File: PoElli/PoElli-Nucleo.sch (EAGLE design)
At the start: 116 parts, among them J3 M022.54MM, J4 M022.54MM, Q3 FDMC2674HANDSOLDERING, Q4 FDMC2674HANDSOLDERING, T1 Coilcraft 230NL, U4 LT3748, U5 TPS2378, U6 ENC424J600, X1 POE-TP-SHIELDED-LEDSTE1888250, Y1 25 MHz

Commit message: tentative layout
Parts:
- removed D10, D14, D15, D16, D17, D7, D8, D9: B2100, ELL-i-DIscreteSemi:DIODE-SCHOTTKYB2100
- added C10: 1nF 2kV, ELL-i-Passives:C1206-A
- added C3: 100nF, ELL-i-Passives:C0805-A
- added U$3, U$4: BRIDGE-RECTIFIER, ELL-i-DIscreteSemi:BRIDGE-RECTIFIER
- C11, C15: device ELL-i-Passives:C0402 -> ELL-i-Passives:C0402-B
- C34: device ELL-i-Passives:C0402-B -> ELL-i-Passives:C0805-A
- R23, R5: device ELL-i-Passives:R0603 -> ELL-i-Passives:R0805-A
- R29: device ELL-i-Passives:R0805 -> ELL-i-Passives:R0805-A
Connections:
- new net N$9: C10.1, R20.1, R21.1
- net ENC-3V3: now also C3.2
- net GNDA: now also C3.1
- net N$5: no longer R20.1, R21.1
- net N$6: now also U$3.+, U$4.+; no longer D10.C, D7.C, D8.C, D9.C
- net N$8: now also U$3.-, U$4.-; no longer D14.A, D15.A, D16.A, D17.A
- net POE_A+: now also U$3.AC1; no longer D14.C, D7.A
- net POE_A-: now also U$3.AC2; no longer D15.C, D8.A
- net POE_B+: now also U$4.AC1; no longer D10.A, D17.C
- net POE_B-: now also U$4.AC2; no longer D16.C, D9.A
- net SGND: now also C10.2
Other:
- note added: "Separate ESD protection for easier layout"

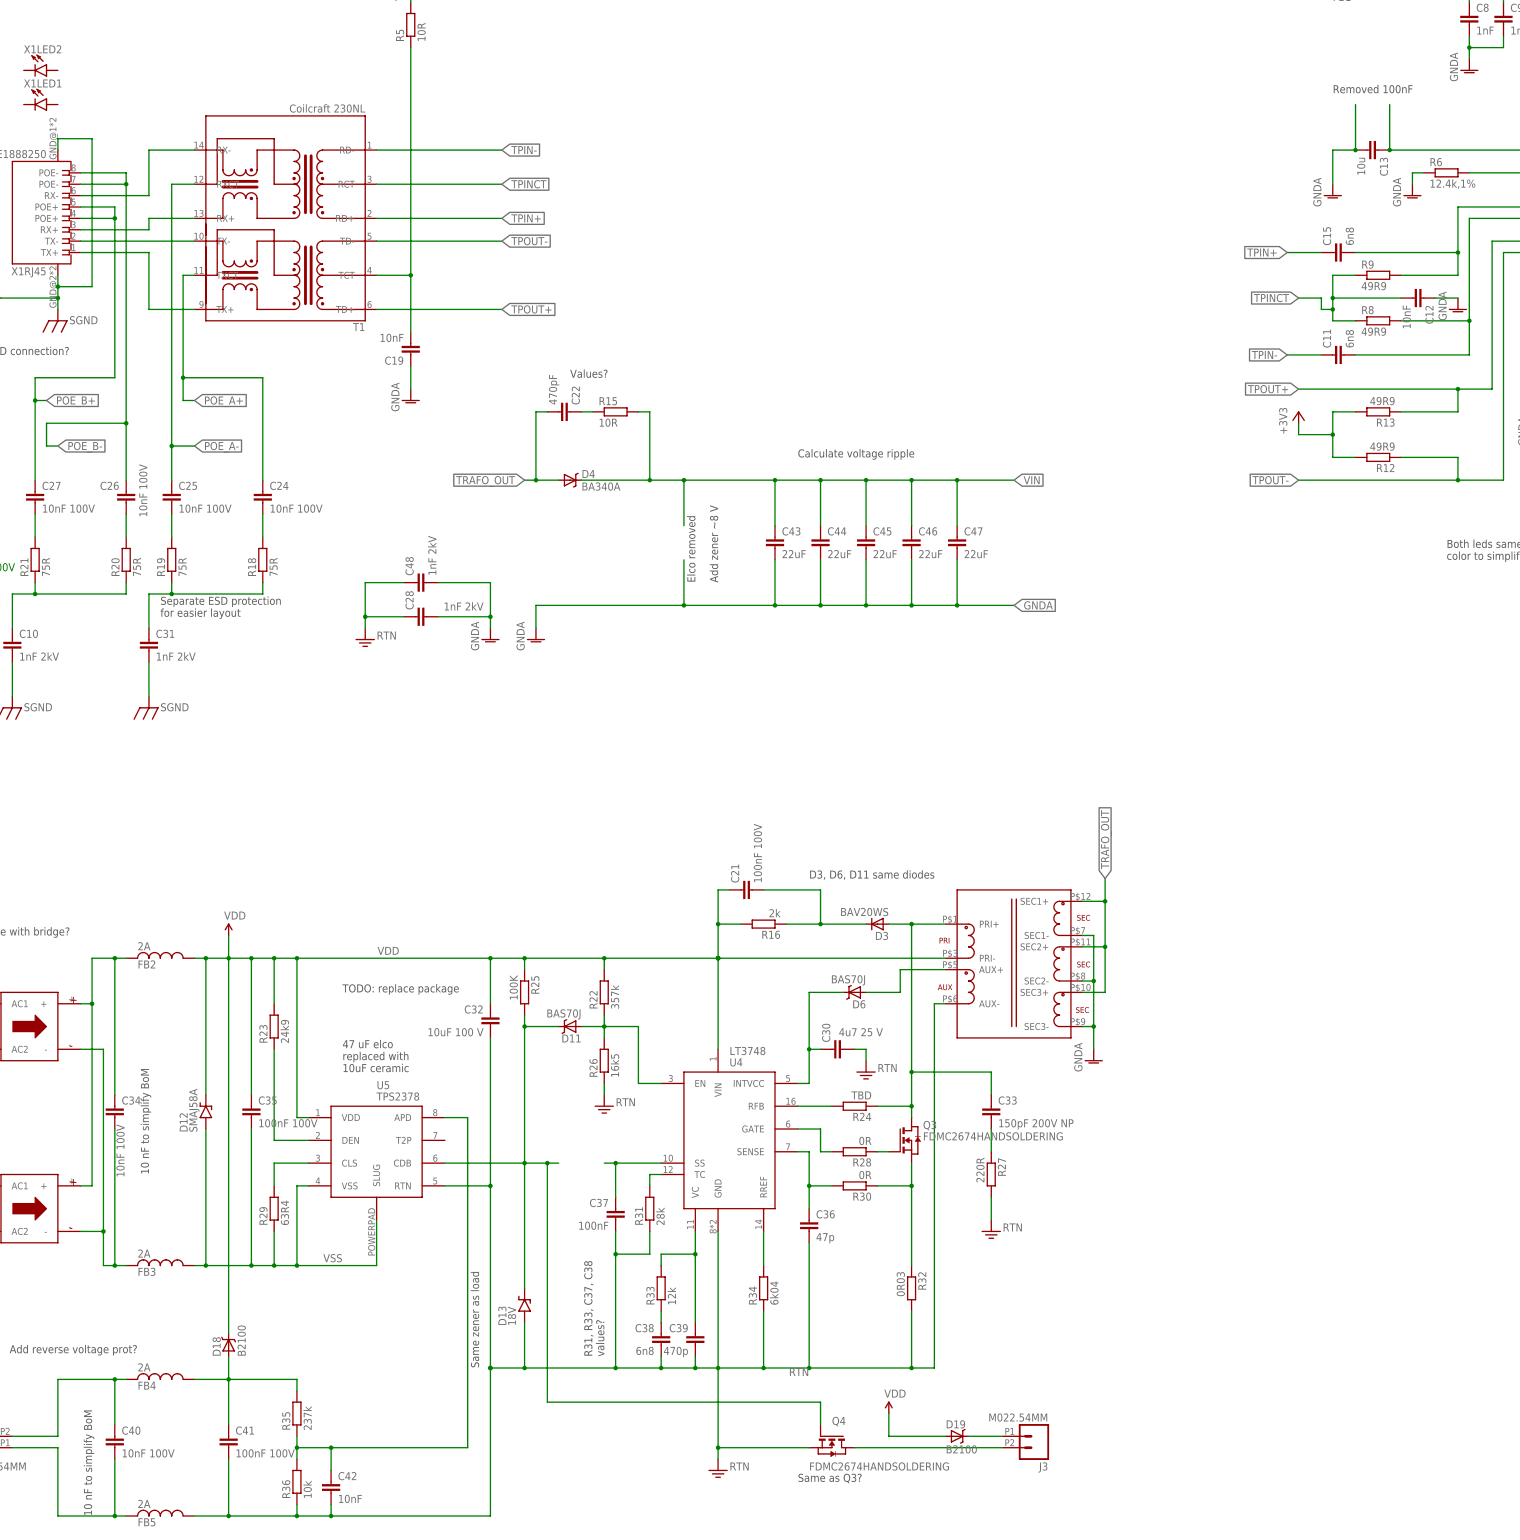
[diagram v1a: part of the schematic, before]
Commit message: Layout, functional blocks placed down
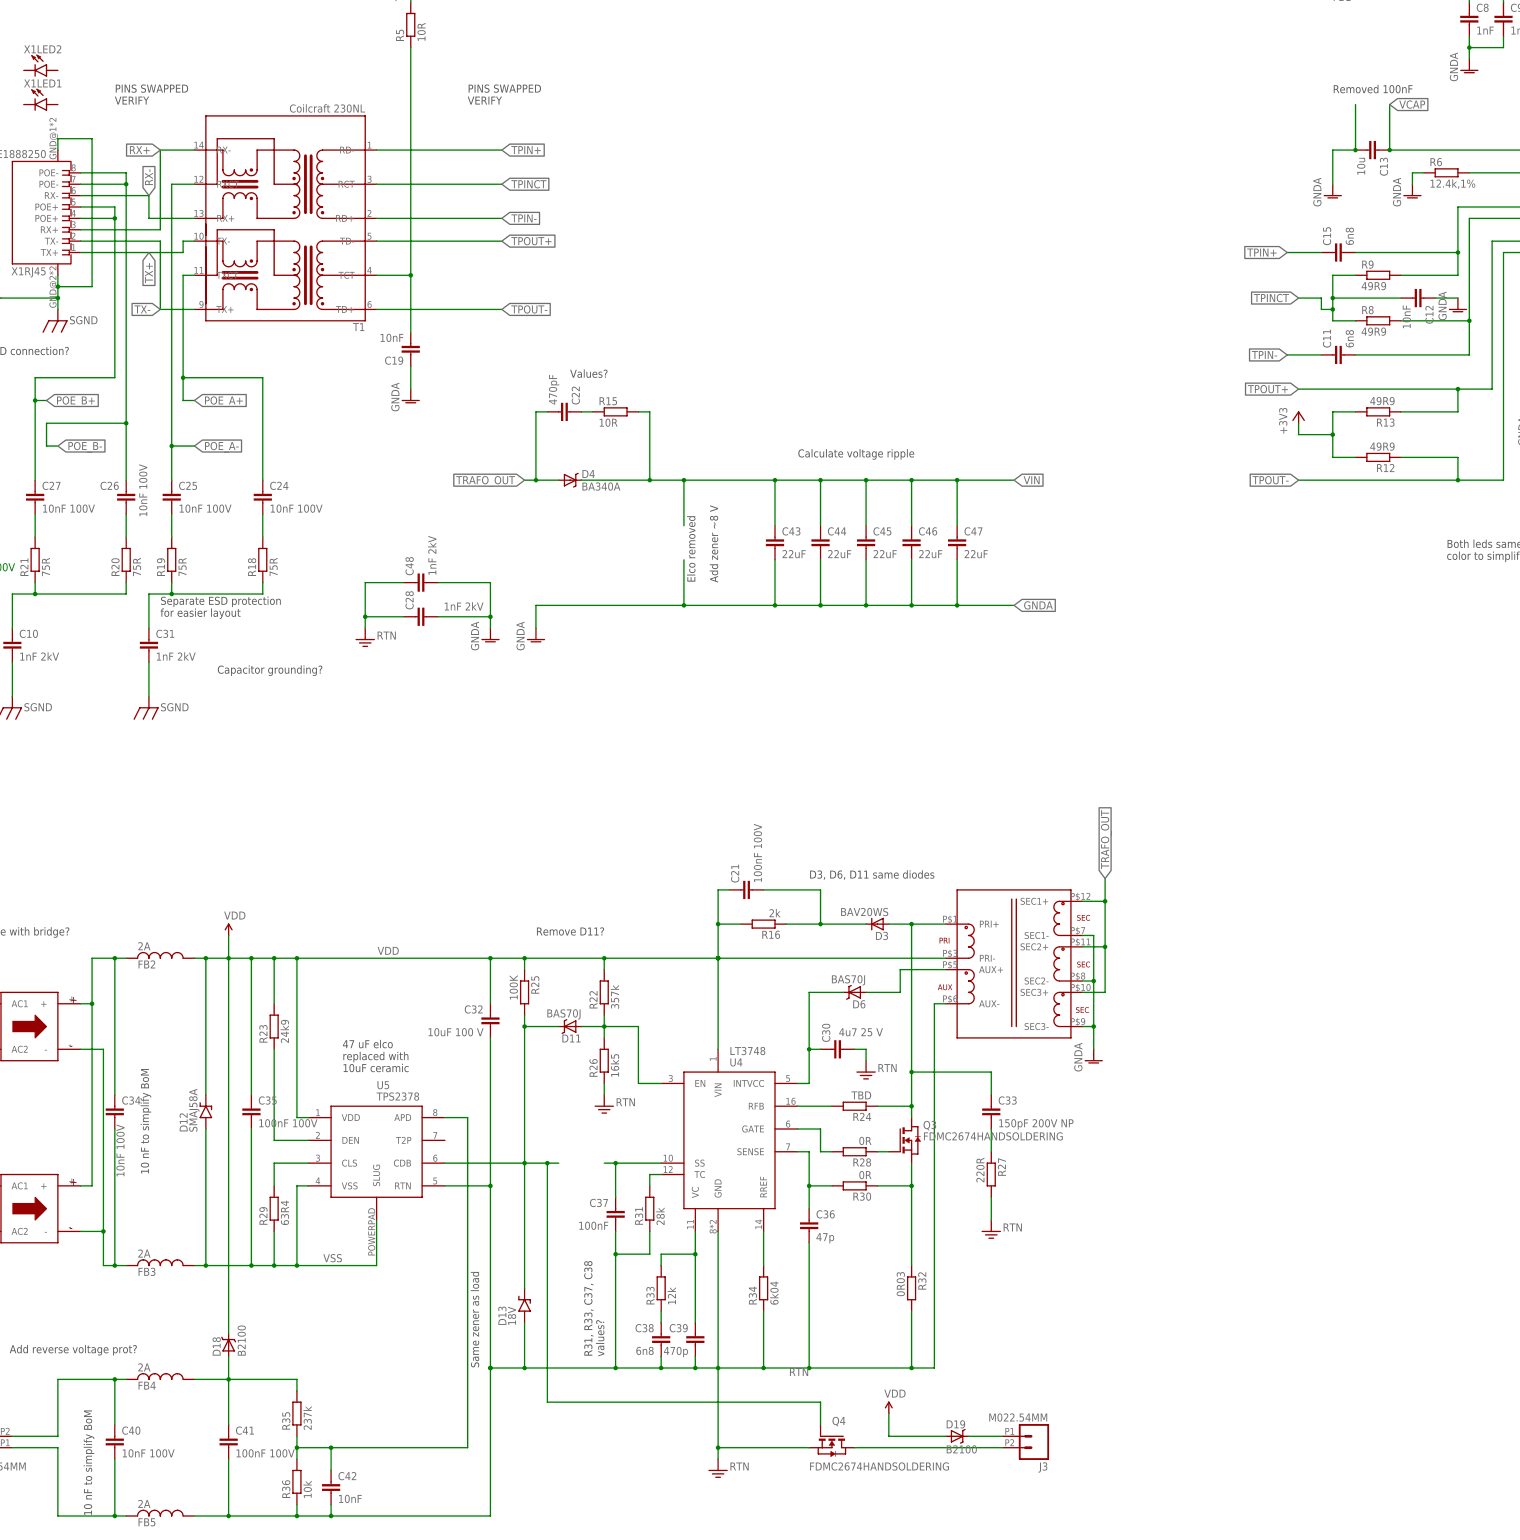
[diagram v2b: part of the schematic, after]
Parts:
- C11, C15: device ELL-i-Passives:C0402-B -> ELL-i-Passives:C0805-A
- C21: device ELL-i-Passives:C0805 -> ELL-i-Passives:C0805-A
- C28, C48: device ELL-i-Passives:CC1206 -> ELL-i-Passives:C1206-A
- C32: device ELL-i-Passives:C1206-A -> ELL-i-Passives:C2220-REFLOW
- FB1: device ELL-i-Passives:FB0402 -> ELL-i-Passives:FB-0805-A
- FB2, FB3, FB5: device ELL-i-Passives:FB1206 -> ELL-i-Passives:FB-0805-A
- FB4: device ELL-i-Passives:FB1206 -> ELL-i-Passives:FB-0603-A
- R16: device ELL-i-Passives:R1206 -> ELL-i-Passives:R1206-A
- R22, R25, R26: device ELL-i-Passives:R0603 -> ELL-i-Passives:R0805-A
- R32: device ELL-i-Passives:R0805 -> ELL-i-Passives:R0805-A
- renumbered U$1 to T2, U$3 to B1, U$4 to B2
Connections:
- removed net N$1: T1.TX-, X1RJ45.TX-@2
- removed net N$2: T1.TX+, X1RJ45.TX+@1
- removed net N$3: T1.RX+, X1RJ45.RX+@3
- removed net N$4: T1.RX-, X1RJ45.RX-@6
- new net RX+: T1.RX-, X1RJ45.RX+@3
- new net RX-: T1.RX+, X1RJ45.RX-@6
- new net TX+: T1.TX-, X1RJ45.TX+@1
- new net TX-: T1.TX+, X1RJ45.TX-@2
- net TPIN+: now also T1.RD-; no longer T1.RD+
- net TPIN-: now also T1.RD+; no longer T1.RD-
- net TPOUT+: now also T1.TD-; no longer T1.TD+
- net TPOUT-: now also T1.TD+; no longer T1.TD-
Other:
- note added: "Capacitor grounding?"
- note added: "PINS SWAPPED VERIFY"
- note added: "Remove D11?"
- note removed: "Same as Q3?"
- note removed: "TODO: replace package"

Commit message: Component placement almost ready
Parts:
- removed C31: 1nF 2kV, ELL-i-Passives:C1206-A
- removed C36: 47p, ELL-i-Passives:C0805-A
- removed D11: BAS70J, ELL-i-DIscreteSemi:BAS70J
- removed R25: 100K, ELL-i-Passives:R0805-A
- removed R30: 0R, ELL-i-Passives:R0805-A
- C1, C11, C12, C13, C15, C2, C21, C22, C24, C25, C26, C27, C3, C30, C33, C34, C35, C37, C38, C39, C4, C41, C42, C5, C6, C7: device ELL-i-Passives:C0805-A -> ELL-i-Passives:C0603-B
- FB2, FB3, FB5: device ELL-i-Passives:FB-0805-A -> ELL-i-Passives:FB-0603-A
- R12, R13, R15, R18, R19, R20, R21, R22, R23, R24, R26, R27, R28, R29, R33, R35, R36, R6, R8, R9: device ELL-i-Passives:R0805-A -> ELL-i-Passives:R0603-B
- R32: value 0R03 -> 0R10; device ELL-i-Passives:R0805-A -> ELL-i-Passives:R0603-B
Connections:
- removed net N$27: Q3.S, R30.1, R32.1
- removed net N$9: C10.1, R20.1, R21.1
- removed net U5_CDB: D11.C, D13.C, Q4.G, R25.2, U5.CDB
- net GNDA: now also C10.2
- net N$26: now also Q3.S, R32.1; no longer C36.1, R30.2
- net N$5: now also C10.1, R20.1, R21.1; no longer C31.1
- net RTN: no longer C36.2
- net SGND: no longer C10.2, C31.2
- net U4_EN: now also D13.C, Q4.G, U5.CDB; no longer D11.A
- net VDD: no longer R25.1
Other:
- note added: "Ilim = 1A"
- note added: "Recalculate R22"
- note added: "Removed R25, D11"
- note added: "Removed RC"
- note added: "SGND left floating"
- note removed: "Remove D11?"
- note removed: "SGND connection?"
- note removed: "Separate ESD protection for easier layout"

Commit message: DC/DC layout except planes
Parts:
- C19: device ELL-i-Passives:C0805-A -> ELL-i-Passives:C0603-B
- R3, R4: device ELL-i-Passives:R0805-A -> ELL-i-Passives:R0603-A
- R31, R34, R5: device ELL-i-Passives:R0805-A -> ELL-i-Passives:R0603-B
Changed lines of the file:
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@@
 <grid distance="0.1" unitdist="inch" unit="inch" style="lines" multiple="1" display="no" altdistance="0.01" altunitdist="inch" altunit="inch"/>
 <layers>
-<layer number="1" name="Top" color="4" fill="1" visible="yes" active="no"/>
-<layer number="2" name="Route2" color="4" fill="15" visible="yes" active="no"/>
-<layer number="3" name="Route3" color="4" fill="3" visible="yes" active="no"/>
-<layer number="14" name="Route14" color="1" fill="6" visible="yes" active="no"/>
-<layer number="15" name="Route15" color="1" fill="15" visible="yes" active="no"/>
-<layer number="16" name="Bottom" color="1" fill="1" visible="yes" active="no"/>
-<layer number="17" name="Pads" color="2" fill="1" visible="yes" active="no"/>
-<layer number="18" name="Vias" color="2" fill="1" visible="yes" active="no"/>
-<layer number="19" name="Unrouted" color="6" fill="1" visible="yes" active="no"/>
-<layer number="20" name="Dimension" color="15" fill="1" visible="yes" active="no"/>
-<layer number="21" name="tPlace" color="11" fill="1" visible="yes" active="no"/>
-<layer number="22" name="bPlace" color="7" fill="1" visible="yes" active="no"/>
-<layer number="23" name="tOrigins" color="15" fill="1" visible="yes" active="no"/>
-<layer number="24" name="bOrigins" color="15" fill="1" visible="yes" active="no"/>
-<layer number="25" name="tNames" color="11" fill="1" visible="yes" active="no"/>
-<layer number="26" name="bNames" color="7" fill="1" visible="yes" active="no"/>
-<layer number="27" name="tValues" color="7" fill="1" visible="yes" active="no"/>
-<layer number="28" name="bValues" color="7" fill="1" visible="yes" active="no"/>
+<layer number="1" name="Top" color="4" fill="1" visible="no" active="no"/>
+<layer number="2" name="Route2" color="4" fill="15" visible="no" active="no"/>
+<layer number="3" name="Route3" color="4" fill="3" visible="no" active="no"/>
+<layer number="14" name="Route14" color="1" fill="6" visible="no" active="no"/>
+<layer number="15" name="Route15" color="1" fill="15" visible="no" active="no"/>
+<layer number="16" name="Bottom" color="1" fill="1" visible="no" active="no"/>
+<layer number="17" name="Pads" color="2" fill="1" visible="no" active="no"/>
+<layer number="18" name="Vias" color="2" fill="1" visible="no" active="no"/>
+<layer number="19" name="Unrouted" color="6" fill="1" visible="no" active="no"/>
+<layer number="20" name="Dimension" color="15" fill="1" visible="no" active="no"/>
+<layer number="21" name="tPlace" color="11" fill="1" visible="no" active="no"/>
+<layer number="22" name="bPlace" color="7" fill="1" visible="no" active="no"/>
+<layer number="23" name="tOrigins" color="15" fill="1" visible="no" active="no"/>
+<layer number="24" name="bOrigins" color="15" fill="1" visible="no" active="no"/>
+<layer number="25" name="tNames" color="11" fill="1" visible="no" active="no"/>
+<layer number="26" name="bNames" color="7" fill="1" visible="no" active="no"/>
+<layer number="27" name="tValues" color="7" fill="1" visible="no" active="no"/>
+<layer number="28" name="bValues" color="7" fill="1" visible="no" active="no"/>
 <layer number="29" name="tStop" color="7" fill="3" visible="no" active="no"/>
 <layer number="30" name="bStop" color="7" fill="6" visible="no" active="no"/>
@@
 <layer number="35" name="tGlue" color="7" fill="4" visible="no" active="no"/>
 <layer number="36" name="bGlue" color="7" fill="5" visible="no" active="no"/>
-<layer number="37" name="tTest" color="7" fill="1" visible="yes" active="no"/>
-<layer number="38" name="bTest" color="7" fill="1" visible="yes" active="no"/>
+<layer number="37" name="tTest" color="7" fill="1" visible="no" active="no"/>
+<layer number="38" name="bTest" color="7" fill="1" visible="no" active="no"/>
 <layer number="39" name="tKeepout" color="4" fill="11" visible="no" active="no"/>
 <layer number="40" name="bKeepout" color="1" fill="11" visible="no" active="no"/>
@@
 <layer number="44" name="Drills" color="7" fill="1" visible="no" active="no"/>
 <layer number="45" name="Holes" color="7" fill="1" visible="no" active="no"/>
-<layer number="46" name="Milling" color="3" fill="1" visible="yes" active="no"/>
-<layer number="47" name="Measures" color="8" fill="1" visible="yes" active="no"/>
-<layer number="48" name="Document" color="7" fill="1" visible="yes" active="no"/>
-<layer number="49" name="Reference" color="7" fill="1" visible="yes" active="no"/>
-<layer number="50" name="dxf" color="7" fill="1" visible="yes" active="no"/>
-<layer number="51" name="tDocu" color="1" fill="1" visible="yes" active="no"/>
-<layer number="52" name="bDocu" color="7" fill="1" visible="yes" active="no"/>
-<layer number="53" name="tGND_GNDA" color="7" fill="9" visible="yes" active="no"/>
-<layer number="54" name="bGND_GNDA" color="1" fill="9" visible="yes" active="no"/>
-<layer number="56" name="wert" color="7" fill="1" visible="yes" active="no"/>
-<layer number="57" name="tCopper" color="7" fill="1" visible="yes" active="no"/>
-<layer number="58" name="bCopper" color="7" fill="1" visible="yes" active="no"/>
+<layer number="46" name="Milling" color="3" fill="1" visible="no" active="no"/>
+<layer number="47" name="Measures" color="8" fill="1" visible="no" active="no"/>
+<layer number="48" name="Document" color="7" fill="1" visible="no" active="no"/>
+<layer number="49" name="Reference" color="7" fill="1" visible="no" active="no"/>
+<layer number="50" name="dxf" color="7" fill="1" visible="no" active="no"/>
+<layer number="51" name="tDocu" color="1" fill="1" visible="no" active="no"/>
+<layer number="52" name="bDocu" color="7" fill="1" visible="no" active="no"/>
+<layer number="53" name="tGND_GNDA" color="7" fill="9" visible="no" active="no"/>
+<layer number="54" name="bGND_GNDA" color="1" fill="9" visible="no" active="no"/>
+<layer number="56" name="wert" color="7" fill="1" visible="no" active="no"/>
+<layer number="57" name="tCopper" color="7" fill="1" visible="no" active="no"/>
+<layer number="58" name="bCopper" color="7" fill="1" visible="no" active="no"/>
 <layer number="91" name="Nets" color="2" fill="1" visible="yes" active="yes"/>
 <layer number="92" name="Busses" color="1" fill="1" visible="yes" active="yes"/>
@@
 <part name="C37" library="ELL-i-Passives" deviceset="C" device="0603-B" value="100nF"/>
 <part name="U4" library="ELL-i-PowerIC" deviceset="LT3748" device=""/>
-<part name="R31" library="ELL-i-Passives" deviceset="R" device="0805-A" value="28k"/>
+<part name="R31" library="ELL-i-Passives" deviceset="R" device="0603-B" value="28k"/>
 <part name="R33" library="ELL-i-Passives" deviceset="R" device="0603-B" value="12k"/>
 <part name="C38" library="ELL-i-Passives" deviceset="C" device="0603-B" value="6n8"/>
@@
 <part name="R24" library="ELL-i-Passives" deviceset="R" device="0603-B" value="TBD"/>
 <part name="C30" library="ELL-i-Passives" deviceset="C" device="0603-B" value="4u7 25 V"/>
-<part name="R34" library="ELL-i-Passives" deviceset="R" device="0805-A" value="6k04"/>
+<part name="R34" library="ELL-i-Passives" deviceset="R" device="0603-B" value="6k04"/>
 <part name="D3" library="ELL-i-DIscreteSemi" deviceset="BAV20WS" device=""/>
 <part name="R16" library="ELL-i-Passives" deviceset="R" device="1206-A" value="2k"/>
@@
 <part name="GND6" library="supply1" deviceset="GNDA" device=""/>
 <part name="GND7" library="supply1" deviceset="GNDA" device=""/>
-<part name="R4" library="ELL-i-Passives" deviceset="R" device="0805-A" value="220"/>
-<part name="R3" library="ELL-i-Passives" deviceset="R" device="0805-A" value="220"/>
+<part name="R4" library="ELL-i-Passives" deviceset="R" device="0603-A" value="220"/>
+<part name="R3" library="ELL-i-Passives" deviceset="R" device="0603-A" value="220"/>
 <part name="GND8" library="supply1" deviceset="GNDA" device=""/>
 <part name="GND9" library="supply1" deviceset="GNDA" device=""/>
@@
 <part name="R36" library="ELL-i-Passives" deviceset="R" device="0603-B" value="10k"/>
 <part name="D18" library="ELL-i-DIscreteSemi" deviceset="DIODE-SCHOTTKY" device="B2100" value="B2100"/>
-<part name="R5" library="ELL-i-Passives" deviceset="R" device="0805-A" value="10R"/>
-<part name="C19" library="ELL-i-Passives" deviceset="C" device="0805-A" value="10nF"/>
+<part name="R5" library="ELL-i-Passives" deviceset="R" device="0603-B" value="10R"/>
+<part name="C19" library="ELL-i-Passives" deviceset="C" device="0603-B" value="10nF"/>
 <part name="+3V2" library="supply1" deviceset="+3V3" device=""/>
 <part name="GND17" library="supply1" deviceset="GNDA" device=""/>
